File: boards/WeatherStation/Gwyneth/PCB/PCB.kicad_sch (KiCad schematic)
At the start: 1 part, among them U1 ESP32-S3-WROOM-1

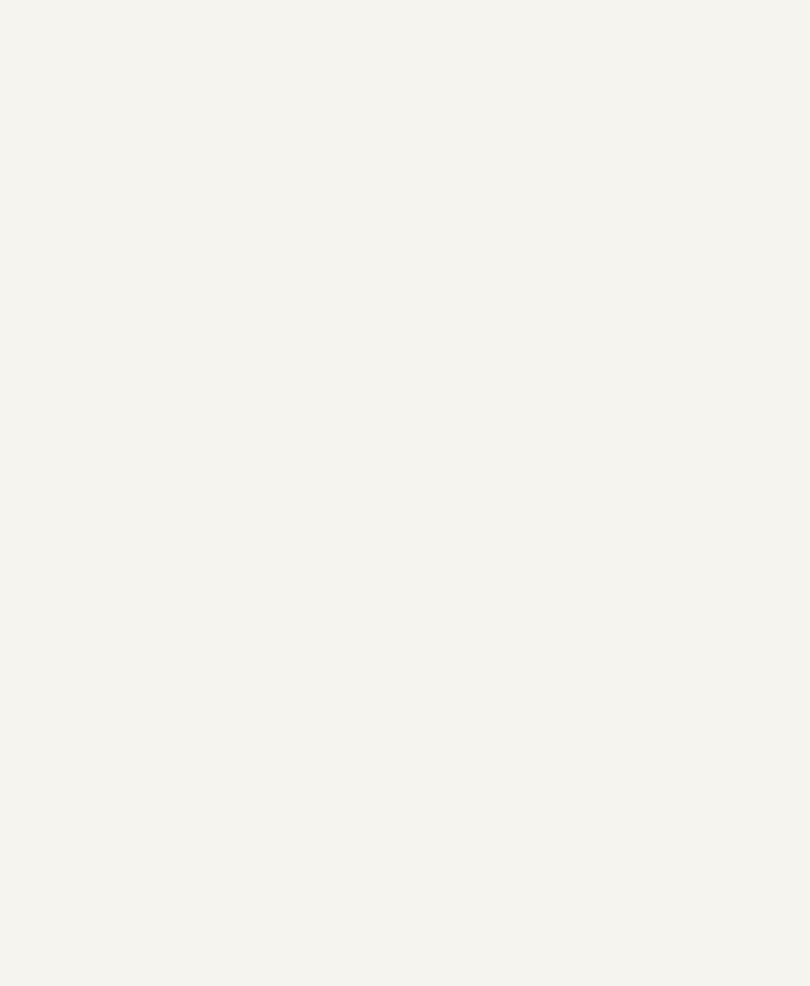
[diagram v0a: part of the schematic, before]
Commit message: Added more sensors
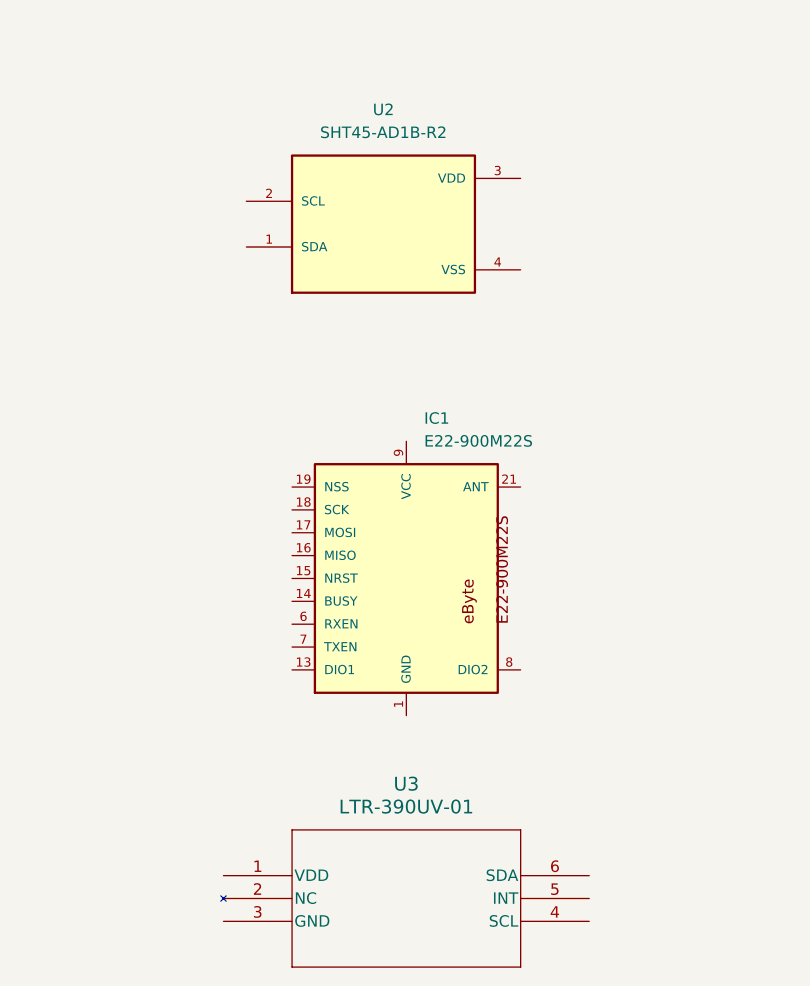
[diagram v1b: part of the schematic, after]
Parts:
- added IC1: E22-900M22S, E22-900M22S:E22-900M22S, symbol E22-900M22S:E22-900M22S
- added U2: SHT45-AD1B-R2, SHT45-AD1B-R2:SHT4X, symbol SHT45-AD1B-R2:SHT45-AD1B-R2
- added U3: LTR-390UV-01, LTR-390UV-01:SMD6_LTR-390UV-01_LTO, symbol LTR-390UV-01:LTR-390UV-01
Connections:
- new net GND: IC1.1 (GND), IC1.10 (GND), IC1.11 (GND), IC1.12 (GND), IC1.2 (GND), IC1.20 (GND), IC1.22 (GND), IC1.3 (GND), IC1.4 (GND), IC1.5 (GND)

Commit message: Edits to schematic
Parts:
- added U5: MLX90614ESF-BAA-000-TU, MLX90614ESF-BAA-000-TU:TO254P942H425-4, symbol MLX90614ESF-BAA-000-TU:MLX90614ESF-BAA-000-TU
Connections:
- no-connect marks 0 -> 1
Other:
- note added: "ESP32"
- note added: "Ebyte Module"
- note added: "Infrared Thermometer"
- note added: "Temperature Sensor"
- note added: "UV Sensor"
- moved on the sheet: U2

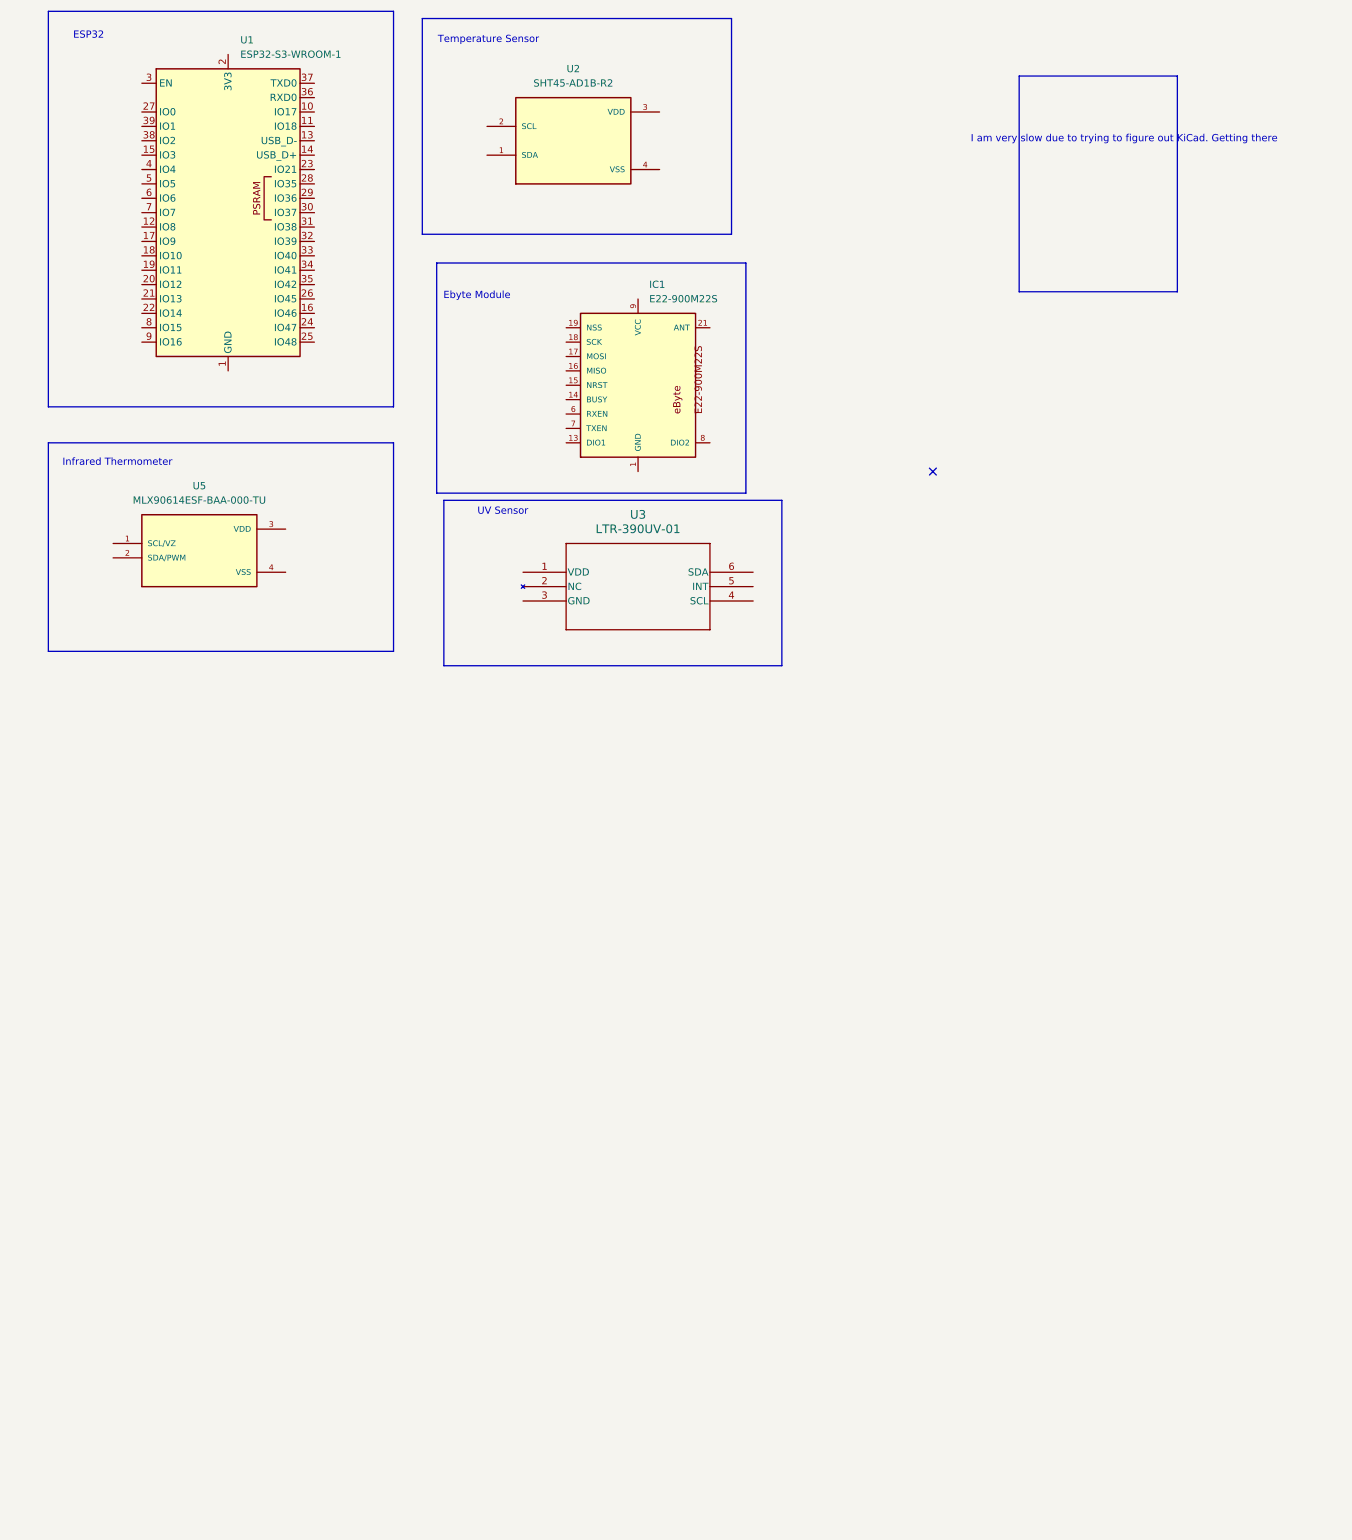
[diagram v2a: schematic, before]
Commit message: added LR2021 and microSD schematic
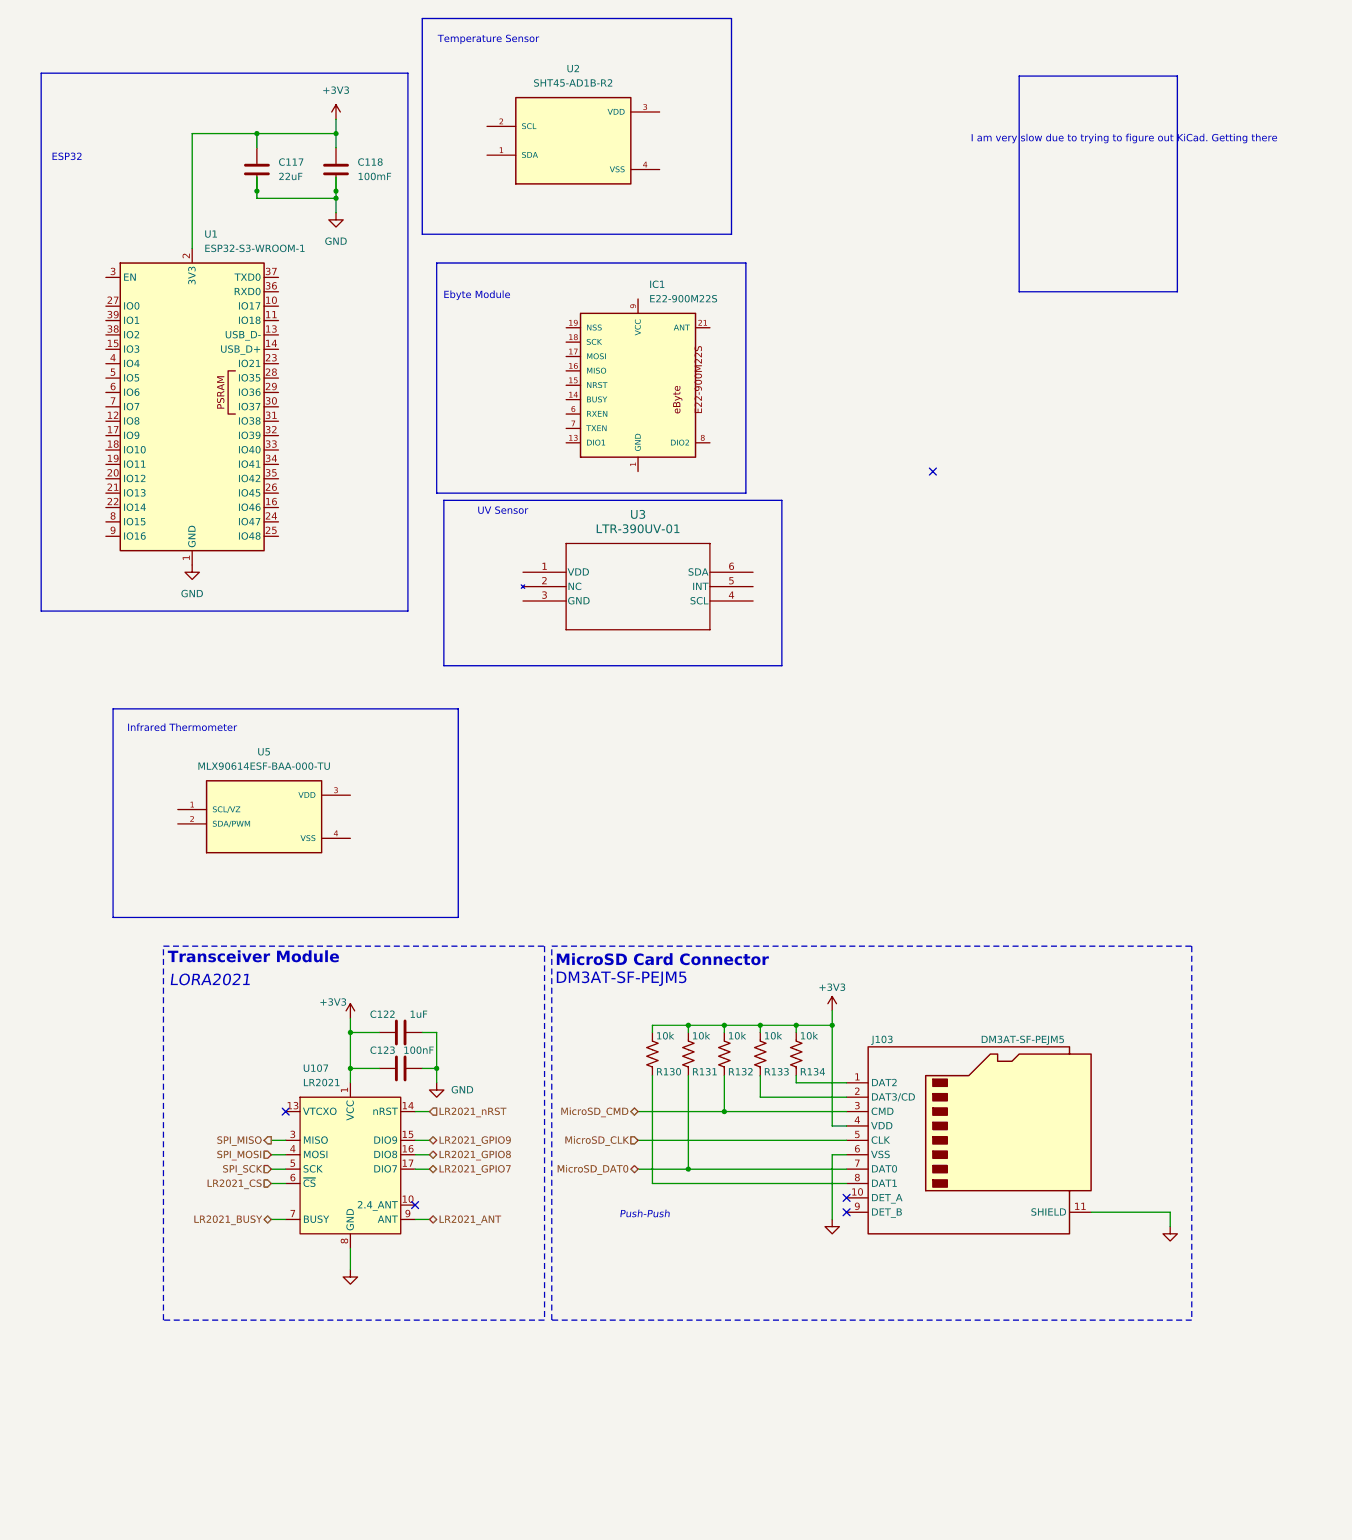
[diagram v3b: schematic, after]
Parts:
- added C117: 22uF, symbol Device:C
- added C118: 100mF, symbol Device:C
- added C122: 1uF, Capacitor_SMD:C_0603_1608Metric, symbol Device:C
- added C123: 100nF, Capacitor_SMD:C_0603_1608Metric, symbol Device:C
- added J103: DM3AT-SF-PEJM5, Connector_Card:microSD_HC_Hirose_DM3AT-SF-PEJM5, symbol Connector:Micro_SD_Card_Det2
- added R130, R131, R132, R133, R134: 10k, Resistor_SMD:R_0603_1608Metric, symbol Device:R_US
- added U107: LR2021, RF_Module_NiceRF:LR2021, symbol Transceiver_NiceRF:LR2021
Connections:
- net GND: now also U1.1 (GND), U1.40 (GND), U1.41 (GND), C117.2, C118.2, C122.2, C123.2, J103.11 (SHIELD), J103.6 (VSS), U107.11 (GND), U107.12 (GND), U107.18 (GND), U107.2 (GND), U107.8 (GND)
- net +3V3: now reaches U1.2 (3V3)
- net +3V3: now also C117.1, C118.1, C122.1, C123.1, J103.4 (VDD), R130.2, R131.2, R132.2, R133.2, R134.2, U107.1 (VCC)
- new net: J103.8 (DAT1), R130.1
- new net: J103.1 (DAT2), R134.1
- new net: J103.2 (DAT3/CD), R133.1
- new net LR2021_ANT: U107.9 (ANT)
- new net LR2021_BUSY: U107.7 (BUSY)
- new net LR2021_CS: U107.6 (~{CS})
- new net LR2021_GPIO7: U107.17 (DIO7)
- new net LR2021_GPIO8: U107.16 (DIO8)
- new net LR2021_GPIO9: U107.15 (DIO9)
- new net LR2021_nRST: U107.14 (nRST)
- new net MicroSD_CLK: J103.5 (CLK)
- new net MicroSD_CMD: J103.3 (CMD), R132.1
- new net MicroSD_DAT0: J103.7 (DAT0), R131.1
- new net SPI_MISO: U107.3 (MISO)
- new net SPI_MOSI: U107.4 (MOSI)
- new net SPI_SCK: U107.5 (SCK)
- no-connect marks 1 -> 5
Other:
- note added: "DM3AT-SF-PEJM5"
- note added: "LORA2021"
- note added: "MicroSD Card Connector"
- note added: "Push-Push"
- note added: "Transceiver Module"
- moved on the sheet: U1, U5

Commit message: infrared thermometer and uv sensor schematic work
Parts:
- added C1, C2: 0.1uF, symbol Device:C
- added C3: 4.7uF, symbol Device:C
- C118: value 100mF -> 0.1uF
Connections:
- net +3V3: now also U3.1 (VDD), U5.3 (VDD), C2.1, C3.1
- net GND: now also U3.3 (GND), U5.4 (VSS), C2.2, C3.2
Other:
- note added: "I01"
- note added: "IO0"
- moved on the sheet: C122, C123, J103, R130, R131, R132, R133, R134, U107, U3, U5

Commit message: added i2c pull up resistors and labels
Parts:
- added R117, R118: 4.7k, Resistor_SMD:R_0402_1005Metric, symbol Device:R_US
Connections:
- net +3V3: now also R117.2, R118.2
- net I2C_SDA: now reaches U1.27 (IO0)
- net I2C_SDA: now also U3.6 (SDA), U5.2 (SDA/PWM), R117.1
- net I2C_SCL: now reaches U1.39 (IO1)
- net I2C_SCL: now also U3.4 (SCL), U5.1 (SCL/VZ), R118.1
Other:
- note added: "Pull-Up Resistors"
- note removed: "I01"
- note removed: "IO0"
